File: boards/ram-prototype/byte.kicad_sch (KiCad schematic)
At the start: 48 parts, among them U1 74LVC1G79, U10 74LVC1G125, U11 74LVC1G79, U12 74LVC1G125, U13 74LVC1G79, U14 74LVC1G125, U15 74LVC1G79, U16 74LVC1G125, U2 74LVC1G125, U3 74LVC1G79, U4 74LVC1G125, U5 74LVC1G79, U6 74LVC1G125, U7 74LVC1G79, U8 74LVC1G125, U9 74LVC1G79

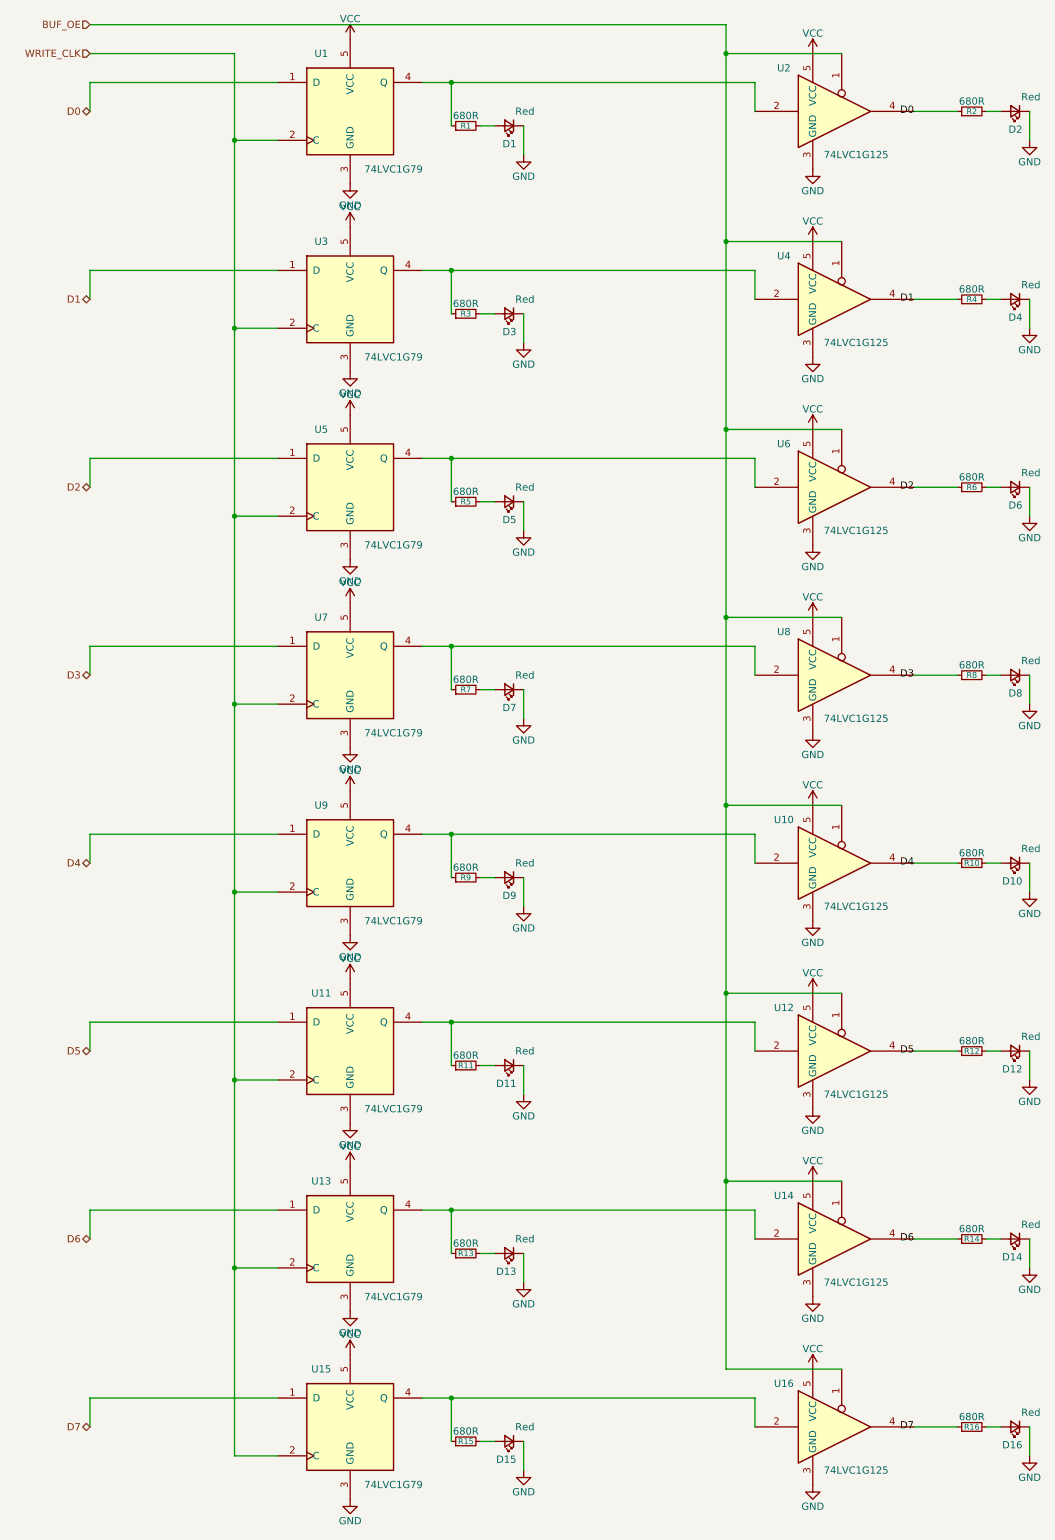
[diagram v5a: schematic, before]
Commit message: fix many issues
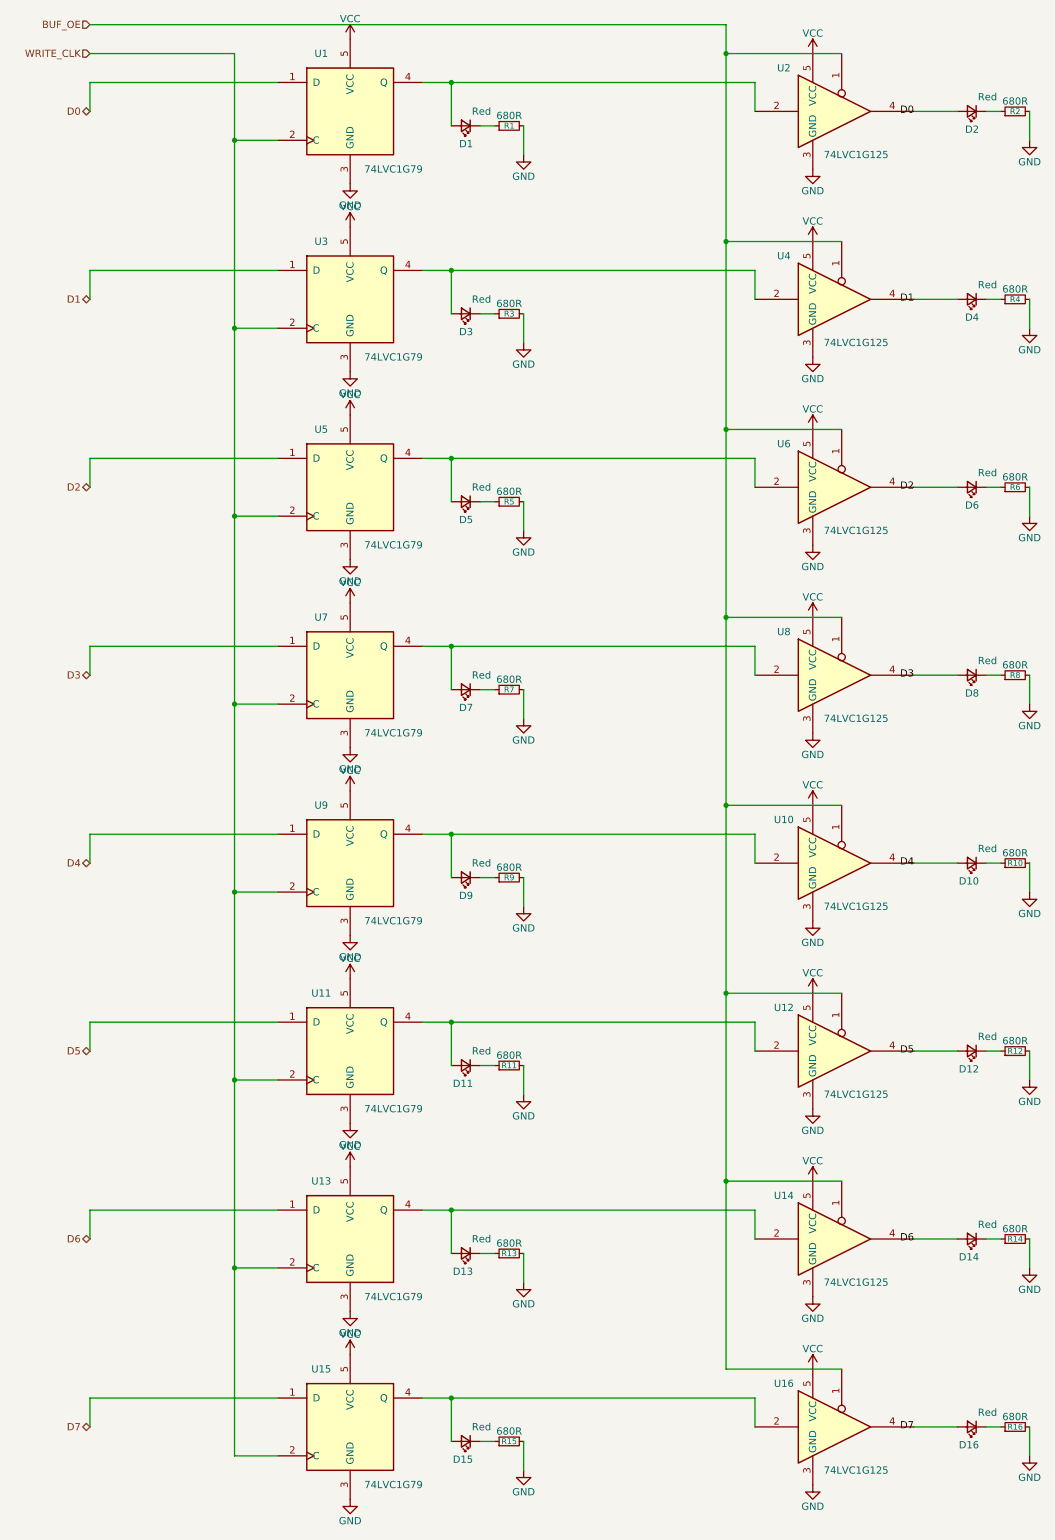
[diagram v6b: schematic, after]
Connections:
- net D0: now also D2.2 (A); no longer R2.1
- net D1: now also D4.2 (A); no longer R4.1
- net D2: now also D6.2 (A); no longer R6.1
- net D3: now also D8.2 (A); no longer R8.1
- net D4: now also D10.2 (A); no longer R10.1
- net D5: now also D12.2 (A); no longer R12.1
- net D6: now also D14.2 (A); no longer R14.1
- net D7: now also D16.2 (A); no longer R16.1
- net GND: now also R1.2, R10.2, R11.2, R12.2, R13.2, R14.2, R15.2, R16.2, R2.2, R3.2, R4.2, R5.2, R6.2, R7.2, R8.2, R9.2; no longer D1.1 (K), D10.1 (K), D11.1 (K), D12.1 (K), D13.1 (K), D14.1 (K), D15.1 (K), D16.1 (K), D2.1 (K), D3.1 (K), D4.1 (K), D5.1 (K), D6.1 (K), D7.1 (K), D8.1 (K), D9.1 (K)
- net at U15.4 (Q), U16.2: now also D15.2 (A); no longer R15.1
- net at U3.4 (Q), U4.2: now also D3.2 (A); no longer R3.1
- net at U11.4 (Q), U12.2: now also D11.2 (A); no longer R11.1
- net at U5.4 (Q), U6.2: now also D5.2 (A); no longer R5.1
- net at U13.4 (Q), U14.2: now also D13.2 (A); no longer R13.1
- net at U1.4 (Q), U2.2: now also D1.2 (A); no longer R1.1
- net at D9.2 (A): now also U10.2, U9.4 (Q); no longer R9.2
- net at U7.4 (Q), U8.2: now also D7.2 (A); no longer R7.1
- new net: D9.1 (K), R9.1
- new net: D13.1 (K), R13.1
- new net: D1.1 (K), R1.1
- new net: D16.1 (K), R16.1
- new net: D7.1 (K), R7.1
- new net: D5.1 (K), R5.1
- new net: D6.1 (K), R6.1
- new net: D3.1 (K), R3.1
- new net: D4.1 (K), R4.1
- new net: D12.1 (K), R12.1
- new net: D11.1 (K), R11.1
- new net: D2.1 (K), R2.1
- new net: D15.1 (K), R15.1
- new net: D10.1 (K), R10.1
- new net: D14.1 (K), R14.1
- new net: D8.1 (K), R8.1

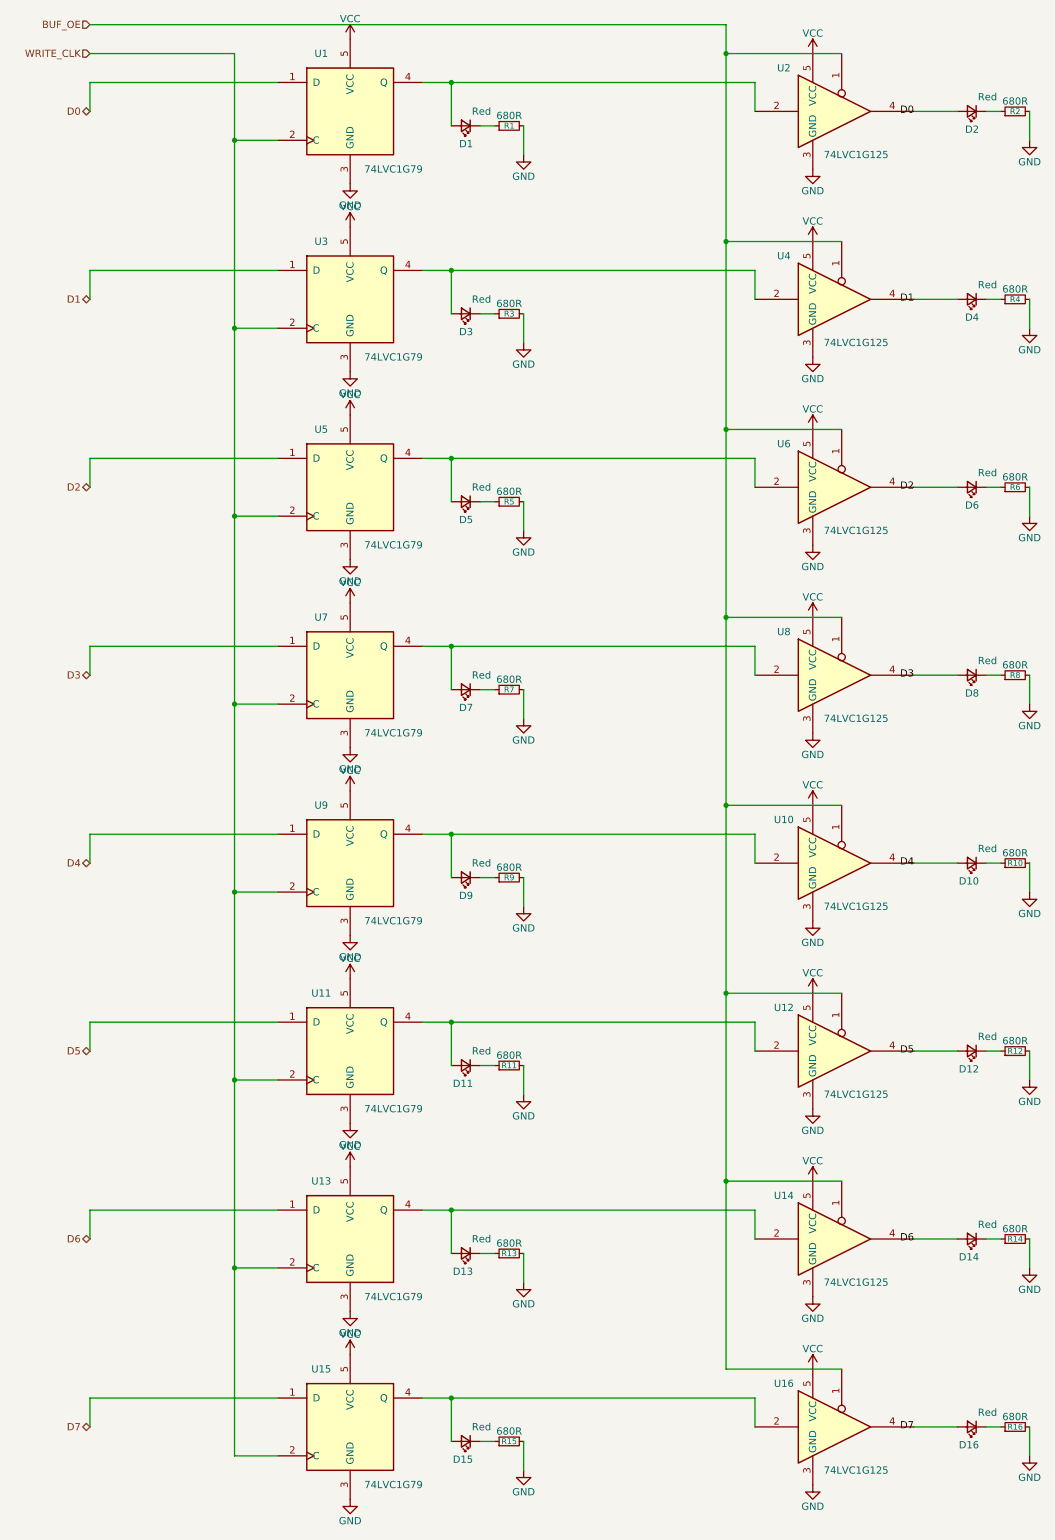
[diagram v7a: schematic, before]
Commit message: Fix some layer issues
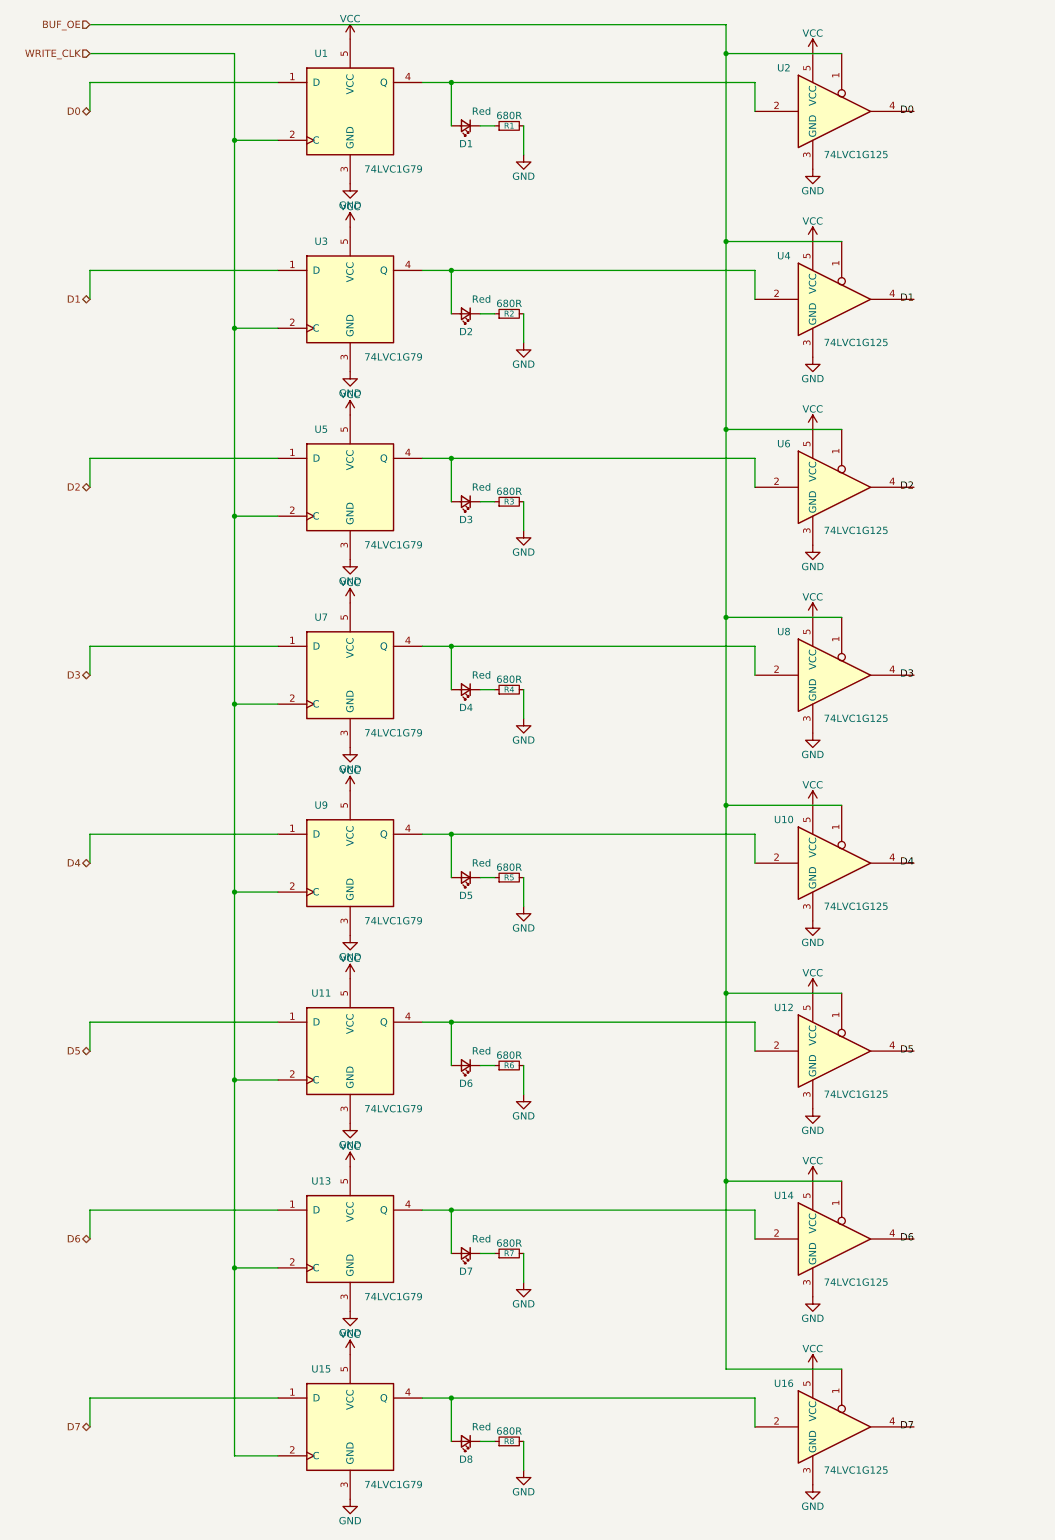
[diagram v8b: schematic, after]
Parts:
- removed D10, D11, D12, D13, D14, D15, D16, D9: Red, symbol Device:LED_Small
- removed R10, R11, R12, R13, R14, R15, R16, R9: 680R, symbol Device:R_Small
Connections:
- net D0: no longer D2.2 (A)
- net D1: no longer D4.2 (A)
- net D2: no longer D6.2 (A)
- net D3: no longer D8.2 (A)
- net at U13.4 (Q), U14.2: now also D7.2 (A)
- net at U5.4 (Q), U6.2: now also D3.2 (A); no longer D5.2 (A)
- net at U11.4 (Q), U12.2: now also D6.2 (A)
- net at U10.2, U9.4 (Q): now also D5.2 (A)
- net at U7.4 (Q), U8.2: now also D4.2 (A); no longer D7.2 (A)
- net at U3.4 (Q), U4.2: now also D2.2 (A); no longer D3.2 (A)
- net at U15.4 (Q), U16.2: now also D8.2 (A)
